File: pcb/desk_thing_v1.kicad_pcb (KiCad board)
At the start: 2 copper layers, 100 x 56 mm, 6 parts, among them SW1 RotaryEncoder_Switch, SW2 SW_Push, SW3 SW_Push, SW4 SW_Push, U1 Pico

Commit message: PCB v1.1
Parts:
- added REF**: MountingHole_3.2mm_M3, MountingHole:MountingHole_3.2mm_M3, F.Cu at (129.0, 98.0)
- added REF**: MountingHole_3.2mm_M3, MountingHole:MountingHole_3.2mm_M3, F.Cu at (37.0, 98.0)
- SW2, SW3, SW4: value SW_Push -> SW_Push_LED; footprint Button_Switch_Keyboard:SW_Cherry_MX_1.00u_PCB -> desk_thing_lib:SW_Cherry_MX_1.00u_PCB
- moved SW4 5.09 mm to (92.5, 91.1)
- moved SW3 4.85 mm to (72.5, 91.1)
- moved SW2 4.72 mm to (52.5, 91.1)
- moved OLED1 0.50 mm to (83.4, 63.1)
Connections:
- U1 pad 10: /BTN2 -> unconnected-(U1-GPIO7-Pad10)_1
- U1 pad 11: /BTN3 -> unconnected-(U1-GPIO8-Pad11)
- U1 pad 16: /ROT_A -> /ROT_B
- U1 pad 17: /ROT_B -> /ROT_A
- U1 pad 21: unconnected-(U1-GPIO16-Pad21) -> /LED3
- U1 pad 22: unconnected-(U1-GPIO17-Pad22) -> /BTN3
- U1 pad 24: unconnected-(U1-GPIO18-Pad24) -> /LED2
- U1 pad 25: unconnected-(U1-GPIO19-Pad25) -> /BTN2
- U1 pad 26: unconnected-(U1-GPIO20-Pad26) -> /LED1
- U1 pad 27: unconnected-(U1-GPIO21-Pad27) -> /BTN1
- U1 pad 36: unconnected-(U1-3V3-Pad36) -> +3V3
- U1 pad 37: +3V3 -> unconnected-(U1-3V3_EN-Pad37)_1
- U1 pad 9: /BTN1 -> unconnected-(U1-GPIO6-Pad9)
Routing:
- net +3V3: track 86.3 -> 0.00 mm
- net /BTN3: track 58.5 -> 19.9 mm
- net /LED1: track 0.00 -> 31.1 mm
- net /LED3: track 0.00 -> 30.0 mm
- net /LED2: track 0.00 -> 26.5 mm
- net /BTN2: track 42.5 -> 18.3 mm
- net /BTN1: track 43.1 -> 27.0 mm
- net /ROT_A: track 86.4 -> 72.8 mm
- net /ROT_B: track 86.0 -> 77.5 mm
- net /OLED_CLK: track 93.4 -> 99.6 mm
- net /OLED_CS: track 89.4 -> 86.2 mm
- net /OLED_DC: track 96.4 -> 94.5 mm
- net /OLED_RESET: track 61.4 -> 60.6 mm
- net GND: vias 2 -> 0
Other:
- board text added: "The Desk Thing v1.1 Ilya Strukov 2024"
- board text removed: "The Desk Thing v1.0 Ilya Strukov 2024"

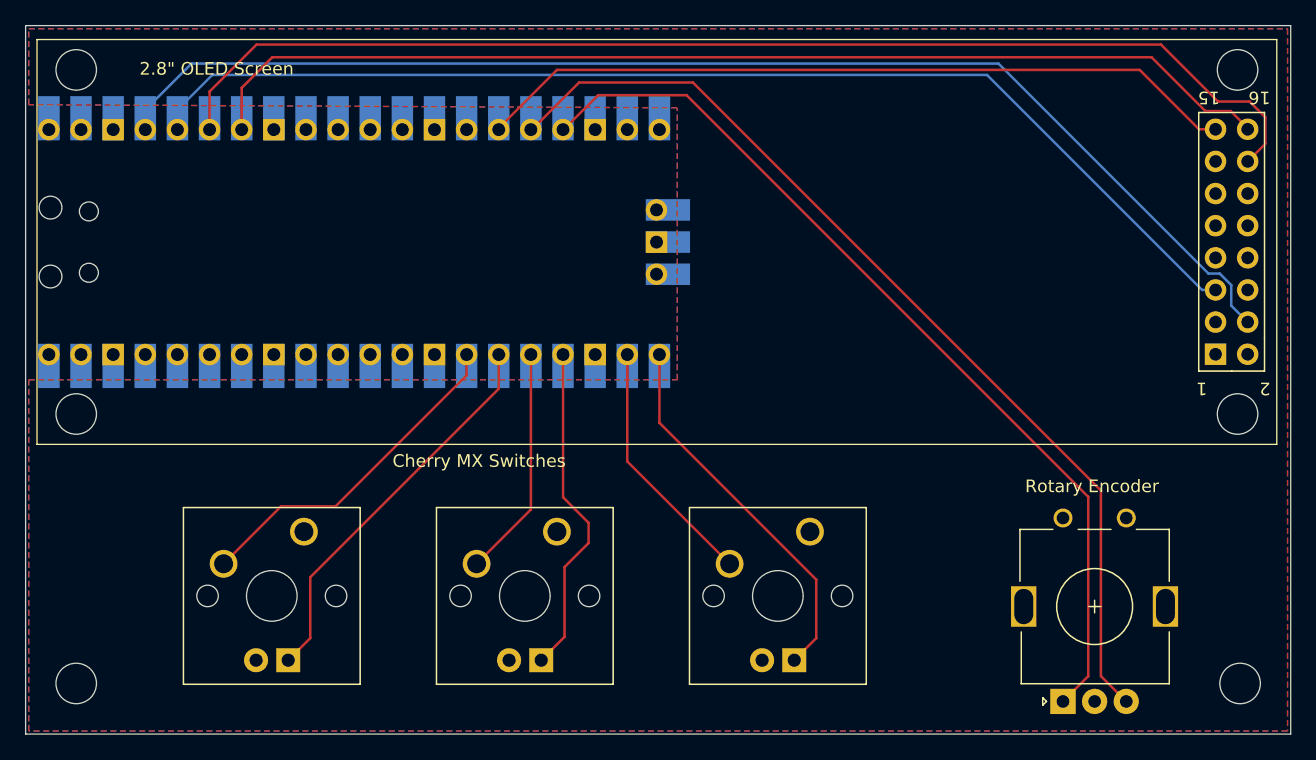
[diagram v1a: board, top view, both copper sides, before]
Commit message: Fix PCB mistakes
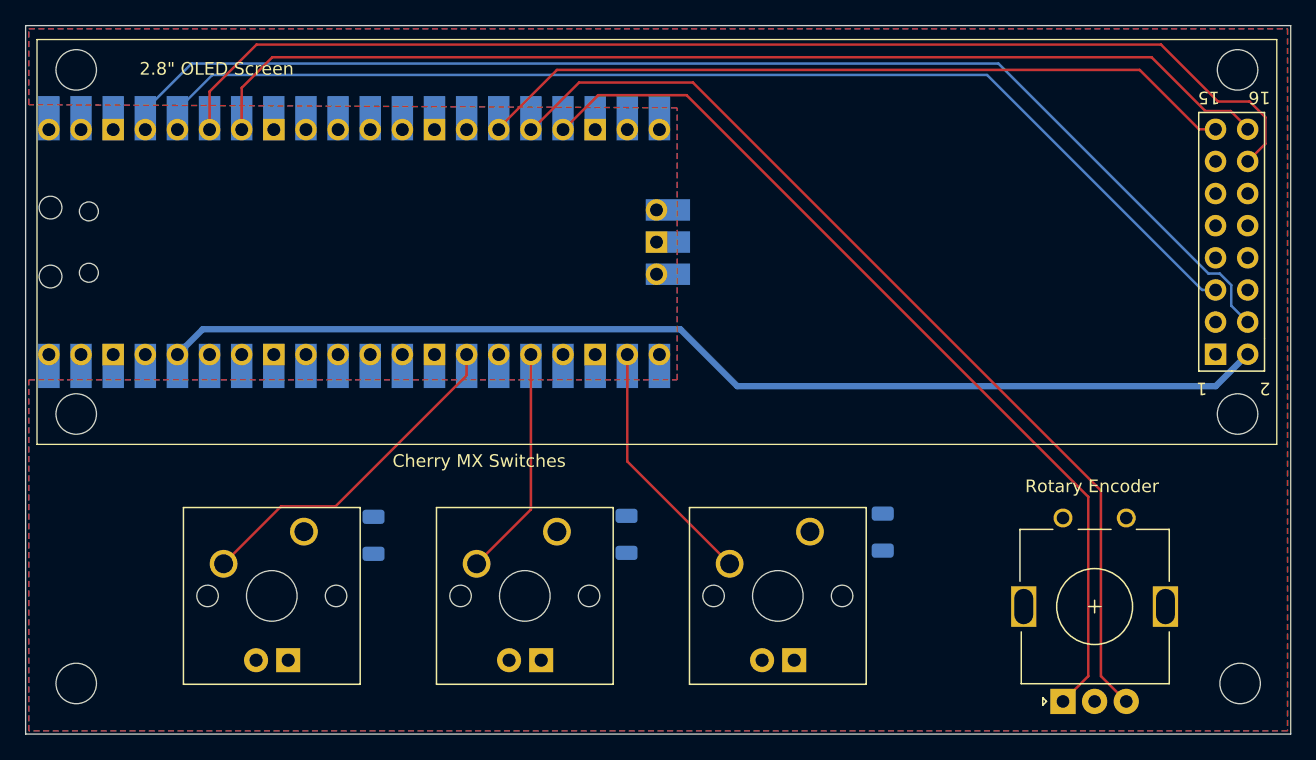
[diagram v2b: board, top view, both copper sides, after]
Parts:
- added R1: R, Resistor_SMD:R_1206_3216Metric, B.Cu at (60.5, 86.3)
- added R2: R, Resistor_SMD:R_1206_3216Metric, B.Cu at (80.5, 86.2)
- added R3: R, Resistor_SMD:R_1206_3216Metric, B.Cu at (100.8, 86.0)
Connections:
- SW2 pad 4: /LED1 -> Net-(SW2-A)
- SW3 pad 4: /LED2 -> Net-(SW3-A)
- SW4 pad 4: /LED3 -> Net-(SW4-A)
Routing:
- net +3V3: track 0.00 -> 88.3 mm
- net /LED1: track 31.1 -> 0.00 mm
- net /LED3: track 30.0 -> 0.00 mm
- net /LED2: track 26.5 -> 0.00 mm
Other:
- board text added: "The Desk Thing v1.2 Ilya Strukov 2024"
- board text removed: "The Desk Thing v1.1 Ilya Strukov 2024"
